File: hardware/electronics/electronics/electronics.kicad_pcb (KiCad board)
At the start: 2 copper layers, 47.5 x 40 mm, 4 parts, among them U2 BME280, U3 ICM-20602, U4 SD Card mini module, U5 ESP32-C3 SUPERMINI

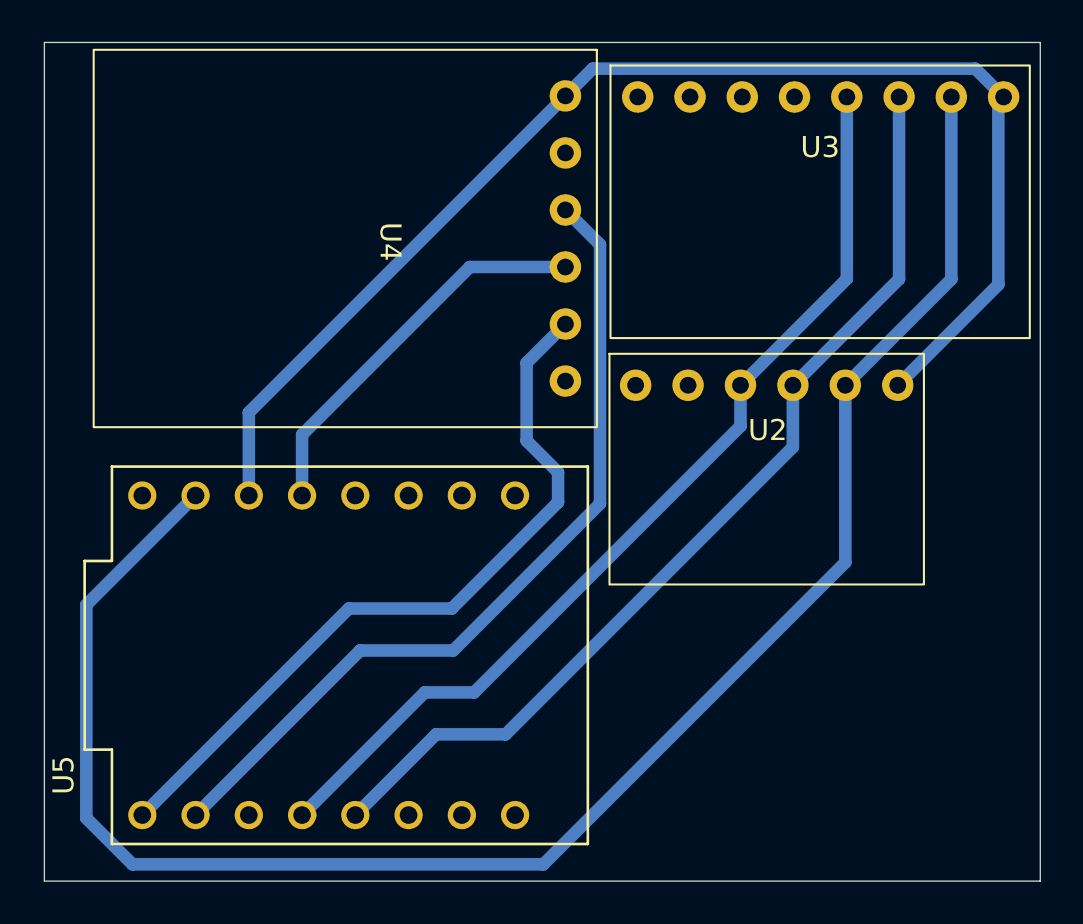
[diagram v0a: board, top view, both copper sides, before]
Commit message: doc: update general documentations
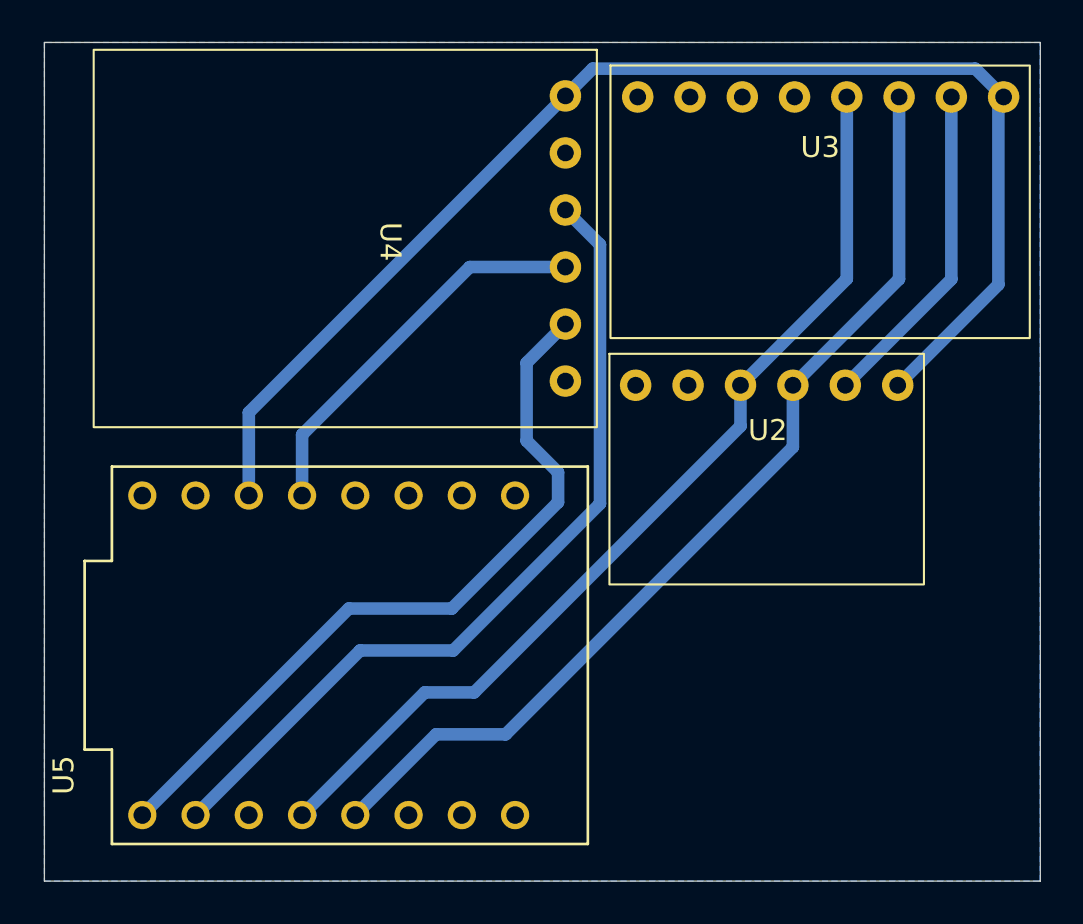
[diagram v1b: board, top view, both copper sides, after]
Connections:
- net /CLK_SD renamed /SCK
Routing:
- net /GND: track 84.9 -> 15.8 mm
- added copper zone on B.Cu, net /GND
